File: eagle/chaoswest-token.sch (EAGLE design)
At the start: 19 parts, among them J1 Amphenol 10118194, Q1 Si1967DH, SW1 AYZ0102AGRLC, U1 MCP73832T-2ACI/OT

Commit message: current status of board (front side quasi final) and some more dxf / xml files added
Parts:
- removed J1: Amphenol 10118194, we-con:USB-MICROB-2
- added U$1, U$2: EMPTY_SIGNAL, extra:EMPTY_SIGNAL
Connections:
- removed net USB-DM: J1.D-
- removed net USB-DP: J1.D+
- new net N$27: U$1.X, U$2.X
- net GND: no longer J1.GND
- net N$22: no longer J1.VBUS
- net N$59: no longer J1.SHIELD
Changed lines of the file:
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@@
 <part name="+3V18" library="supply1" deviceset="+3V3" device=""/>
 <part name="BAT1" library="Keystone-3002" deviceset="3002" device=""/>
-<part name="J1" library="we-con" deviceset="USB" device="-MICROB-2" value="Amphenol 10118194"/>
 <part name="B+" library="testpad" deviceset="TP" device="TP18SQ"/>
 <part name="B-" library="testpad" deviceset="TP" device="TP18SQ"/>
+<part name="U$1" library="extra" deviceset="EMPTY_SIGNAL" device=""/>
+<part name="U$2" library="extra" deviceset="EMPTY_SIGNAL" device=""/>
 </parts>
 <sheets>
@@
 <instance part="+3V18" gate="G$1" x="114.3" y="114.3"/>
 <instance part="BAT1" gate="G$1" x="53.34" y="83.82" rot="R270"/>
-<instance part="J1" gate="J" x="170.18" y="104.14"/>
 <instance part="B+" gate="G$1" x="50.8" y="91.44" rot="R90"/>
 <instance part="B-" gate="G$1" x="50.8" y="76.2" rot="R90"/>
+<instance part="U$1" gate="G$1" x="10.16" y="10.16"/>
+<instance part="U$2" gate="G$1" x="17.78" y="10.16"/>
 </instances>
 <busses>
@@
 <wire x1="154.94" y1="73.66" x2="154.94" y2="101.6" width="0.1524" layer="91"/>
 <pinref part="GND30" gate="1" pin="GND"/>
-<pinref part="J1" gate="J" pin="GND"/>
 <wire x1="154.94" y1="101.6" x2="162.56" y2="101.6" width="0.1524" layer="91"/>
 </segment>
@@
 <segment>
 <label x="157.48" y="106.68" size="1.27" layer="95" rot="R180" xref="yes"/>
-<pinref part="J1" gate="J" pin="D-"/>
 <wire x1="157.48" y1="106.68" x2="162.56" y2="106.68" width="0.1524" layer="91"/>
 </segment>
@@
 <segment>
 <label x="157.48" y="109.22" size="1.27" layer="95" rot="R180" xref="yes"/>
-<pinref part="J1" gate="J" pin="D+"/>
 <wire x1="157.48" y1="109.22" x2="162.56" y2="109.22" width="0.1524" layer="91"/>
 </segment>
@@
 <pinref part="C5" gate="G$1" pin="1"/>
 <pinref part="R5" gate="G$1" pin="2"/>
-<pinref part="J1" gate="J" pin="SHIELD"/>
 <wire x1="167.64" y1="83.82" x2="167.64" y2="96.52" width="0.1524" layer="91"/>
 </segment>
@@
 <pinref part="C1" gate="G$1" pin="1"/>
 <pinref part="L1" gate="G$1" pin="1"/>
-<pinref part="J1" gate="J" pin="VBUS"/>
 </segment>
 </net>
@@
 </segment>
 </net>
+<net name="N$27" class="0">
+<segment>
+<pinref part="U$1" gate="G$1" pin="X"/>
+<pinref part="U$2" gate="G$1" pin="X"/>
+<wire x1="10.16" y1="10.16" x2="17.78" y2="10.16" width="0.1524" layer="91"/>
+</segment>
+</net>

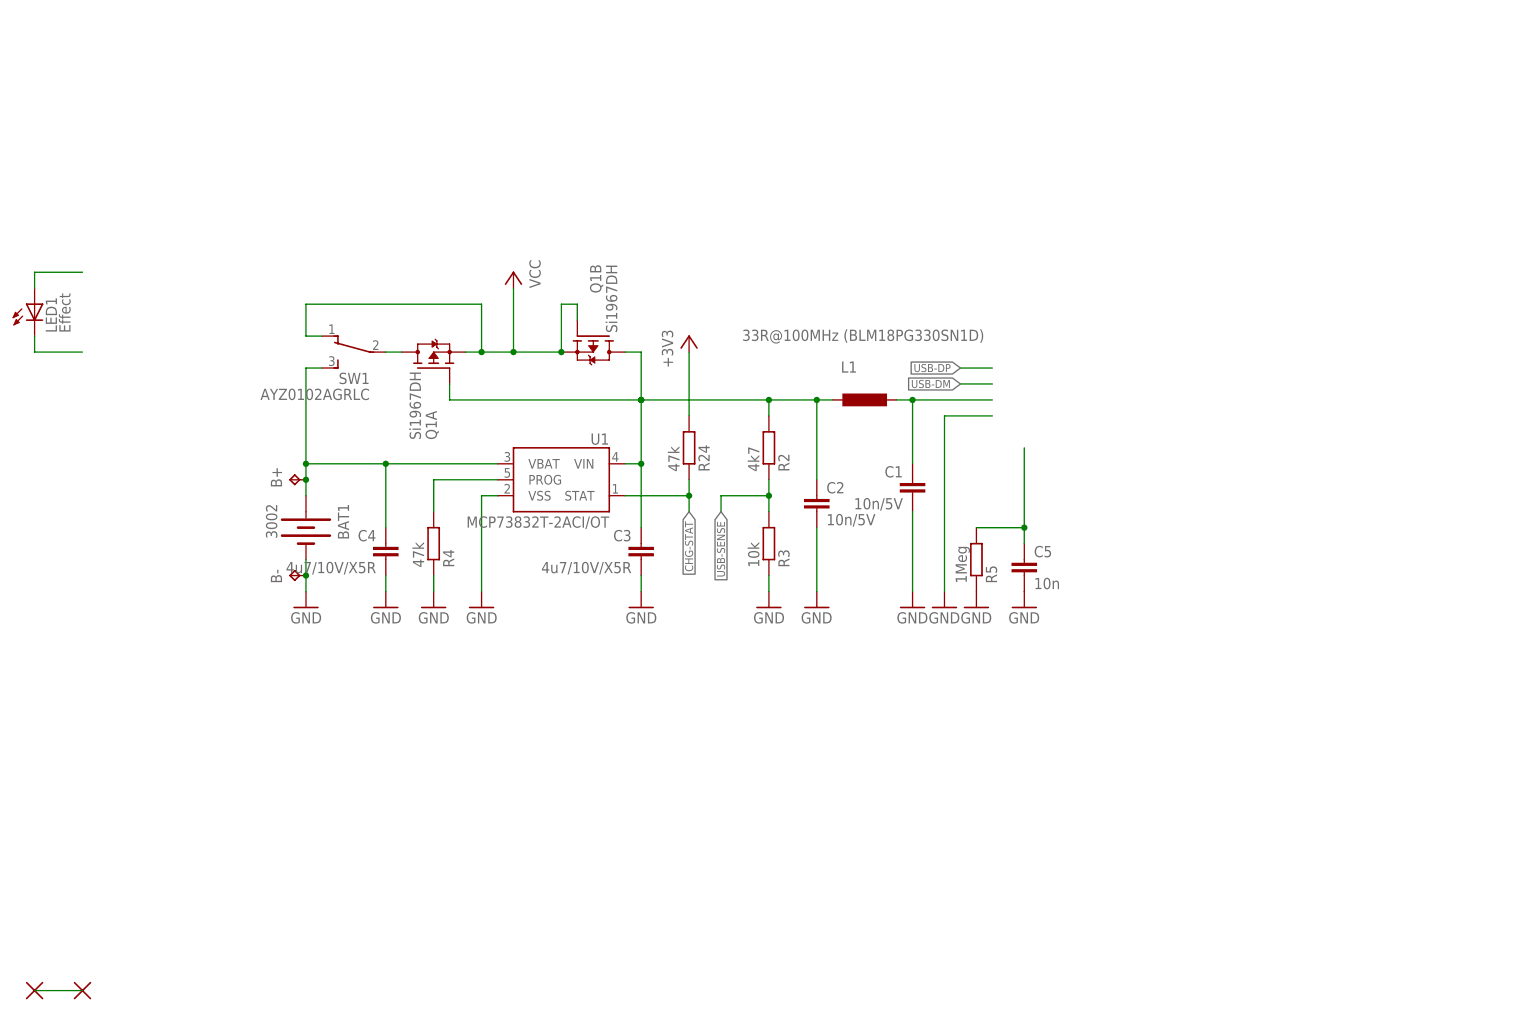
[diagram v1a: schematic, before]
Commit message: schematic should be mostly done, routing is in process, 42 airwires left
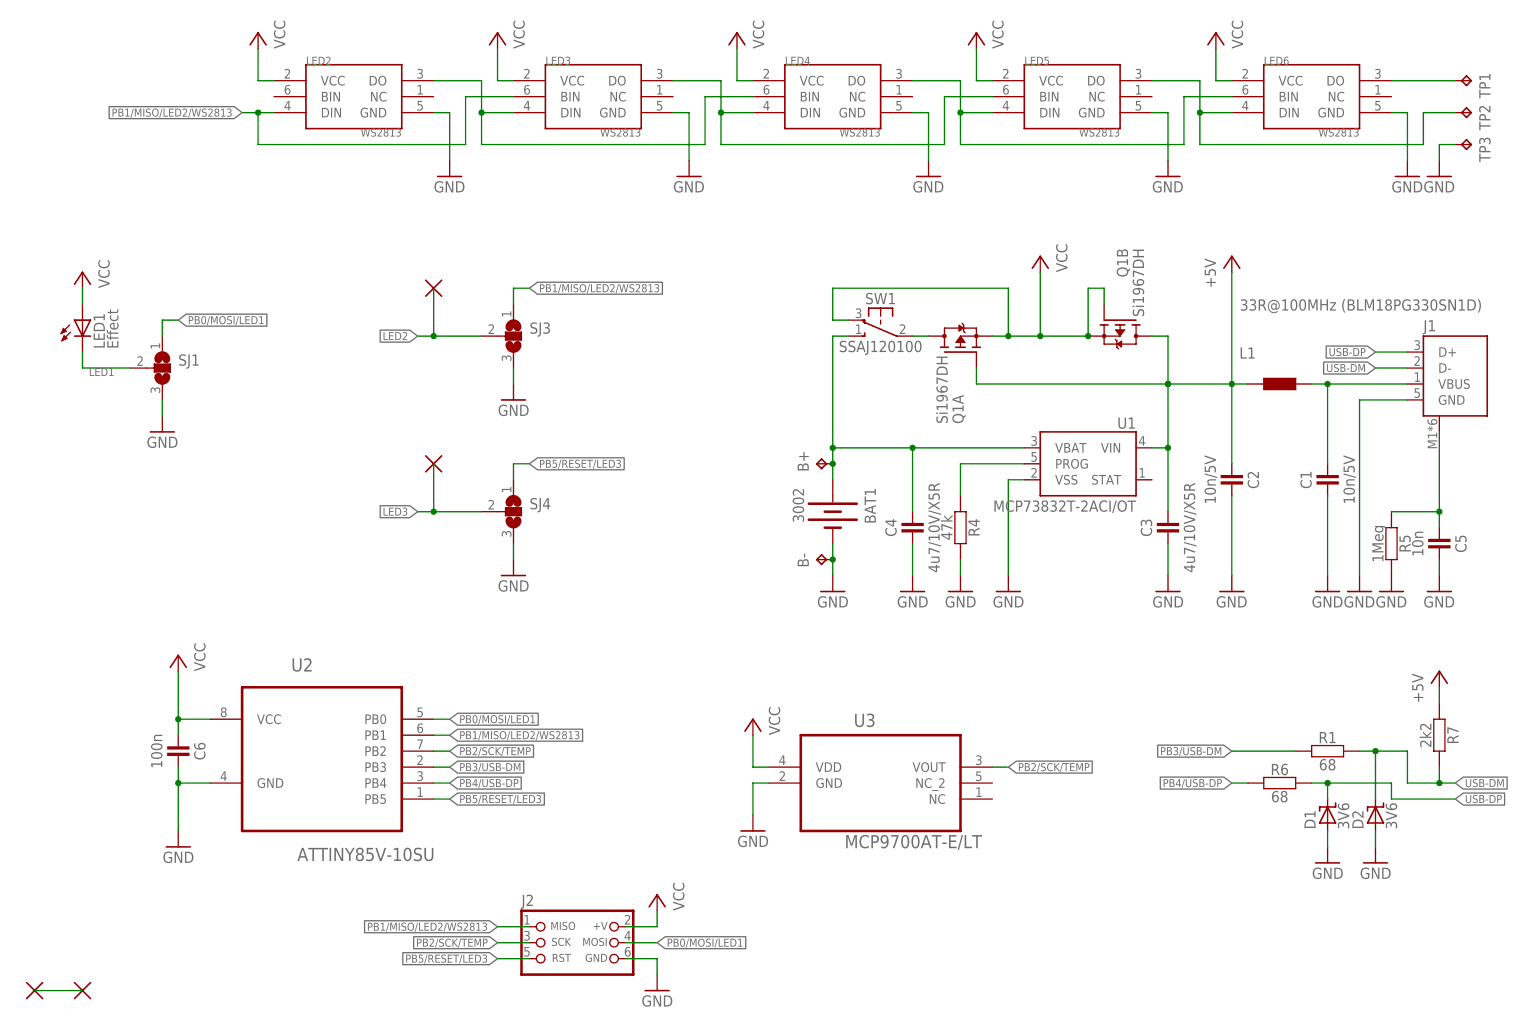
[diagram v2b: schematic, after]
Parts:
- removed R2: 4k7, rcl:R-EU_R0603
- removed R24: 47k, rcl:R-EU_R0603
- removed R3: 10k, rcl:R-EU_R0603
- added C6: 100n, we-rcl:CAPACITOR-0805
- added D1, D2: 3V6, we-rcl:D_ZENER-SOD123
- added J1: (no value), Molex-47346-0001:47346-0001
- added J2: CON_HEADER_PRG_AVR_ICSP-SMD, dp_devices:CON_HEADER_PRG_AVR_ICSP-SMD
- added LED2, LED3, LED4, LED5, LED6: WS2813, extra:WS2813
- added R1, R6: 68, we-rcl:RESISTOR-0805
- added R7: 2k2, we-rcl:RESISTOR-0805
- added SJ1, SJ3, SJ4: (no value), jumper:SJ2W
- added TP1: DO, testpad:TPTP09SQ
- added TP2: BO, testpad:TPTP09SQ
- added TP3: GND, testpad:TPTP09SQ
- added U$3, U$4: EMPTY_SIGNAL, extra:EMPTY_SIGNAL
- added U2: ATTINY85V-10SU, Atmel-ATTINY85V-10SU:ATTINY85V-10SU
- added U3: MCP9700AT-E/LT, Microchip_By_element14_Batch_1:MCP9700AT-E/LT
- BAT1: device Keystone-3002:3002 -> extra:3002
- C1, C2: device rcl:C-EUC1206K -> we-rcl:CAPACITOR-0805
- C3, C4, C5: device rcl:C-EUC0603K -> we-rcl:CAPACITOR-0805
- L1: device rcl:L-EUL2012C -> we-rcl:INDUCTOR-0805
- R4, R5: device rcl:R-EU_R0603 -> we-rcl:RESISTOR-0805
- SW1: value AYZ0102AGRLC -> SSAJ120100; device C&K-Switch:AYZ0102AGRLC -> extra:SSAJ120100
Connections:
- removed net +3V3: R24.2
- removed net CHG-STAT: R24.1, U1.STAT
- removed net N$22: C1.1, L1.1
- removed net N$23: C2.1, C3.1, L1.2, Q1A.G, Q1B.D, R2.2, U1.VIN
- removed net N$24: Q1A.D, SW1.P
- removed net N$31: B+.TP, BAT1.+, C4.1, SW1.S, U1.VBAT
- removed net USB-SENSE: R2.1, R3.2
- new net +5V: C2.1, C3.1, L1.2, Q1A.G, Q1B.D, R7.2, U1.VIN
- new net LED1: LED1.C, SJ1.2
- new net LED2: SJ3.2, U$3.X
- new net LED3: SJ4.2, U$4.X
- new net N$2: LED2.DO, LED3.DIN, LED4.BIN
- new net N$35: LED4.DO, LED5.DIN, LED6.BIN
- new net N$42: LED5.DO, LED6.DIN, TP2.TP
- new net N$43: LED6.DO, TP1.TP
- new net PB0/MOSI/LED1: J2.MOSI, SJ1.1, U2.PB0
- new net PB1/MISO/LED2/WS2813: J2.MISO, LED2.DIN, LED3.BIN, SJ3.1, U2.PB1
- new net PB2/SCK/TEMP: J2.SCK, U2.PB2, U3.VOUT
- new net PB3/USB-DM: R1.2, U2.PB3
- new net PB4/USB-DP: R6.2, U2.PB4
- new net PB5/RESET/LED3: J2.RST, SJ4.1, U2.PB5
- new net USB-DM: D2.C, J1.D-, R1.1, R7.1
- new net USB-DP: D1.C, J1.D+, R6.1
- new net VBAT: B+.TP, BAT1.+, C4.1, SW1.S1, U1.VBAT
- new net VBUS: C1.1, J1.VBUS, L1.1
- net GND: now also C6.2, D1.A, D2.A, J1.GND, J2.GND, LED2.GND, LED3.GND, LED4.GND, LED5.GND, LED6.GND, SJ1.3, SJ3.3, SJ4.3, TP3.TP, U2.GND, U3.GND; no longer R3.1
- net N$59: now also J1.SHIELD
- net N$6: now also Q1A.D, SW1.P1; no longer LED1.A
- net N$7: now also LED3.DO, LED4.DIN, LED5.BIN; no longer LED1.C
- net VCC: now also C6.1, J2.+V, LED1.A, LED2.VCC, LED3.VCC, LED4.VCC, LED5.VCC, LED6.VCC, SW1.O1, U2.VCC, U3.VDD; no longer SW1.O
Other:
- moved on the sheet: B+, B-, BAT1, LED1, Q1A, Q1B, U1
